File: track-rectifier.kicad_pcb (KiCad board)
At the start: 2 copper layers, 25 x 40 mm, 16 parts, among them J1 PAD, J2 MPB1, J3 Screw_Terminal_01x02, J4 PAD, J5 MPB1

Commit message: Change name to "Track Rectifier".
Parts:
- D3: footprint track-voltage:S250 -> track-rectifier:S250
- J2, J5: footprint track-voltage:MPB1 -> track-rectifier:MPB1
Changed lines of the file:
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@@
     (add_net VCC)
   )
-  (module track-voltage:MPB1 (layer F.Cu)
+  (module track-rectifier:MPB1 (layer F.Cu)
     (at 172.72 91.44 90)
     (fp_text reference J5 (at 5.334 3.302 90) (layer F.SilkS)
@@
       (net 6 /K) (zone_connect 2))
   )
-  (module track-voltage:MPB1 (layer F.Cu)
+  (module track-rectifier:MPB1 (layer F.Cu)
     (at 192.405 91.44 90)
     (fp_text reference J2 (at 5.334 -3.048 90) (layer F.SilkS)
@@
       (net 4 /J) (zone_connect 2))
   )
-  (module track-voltage:S250 (layer F.Cu)
+  (module track-rectifier:S250 (layer F.Cu)
     (at 182.372 102.362 270)
     (fp_text reference D3 (at 0 4.318 180) (layer F.SilkS)

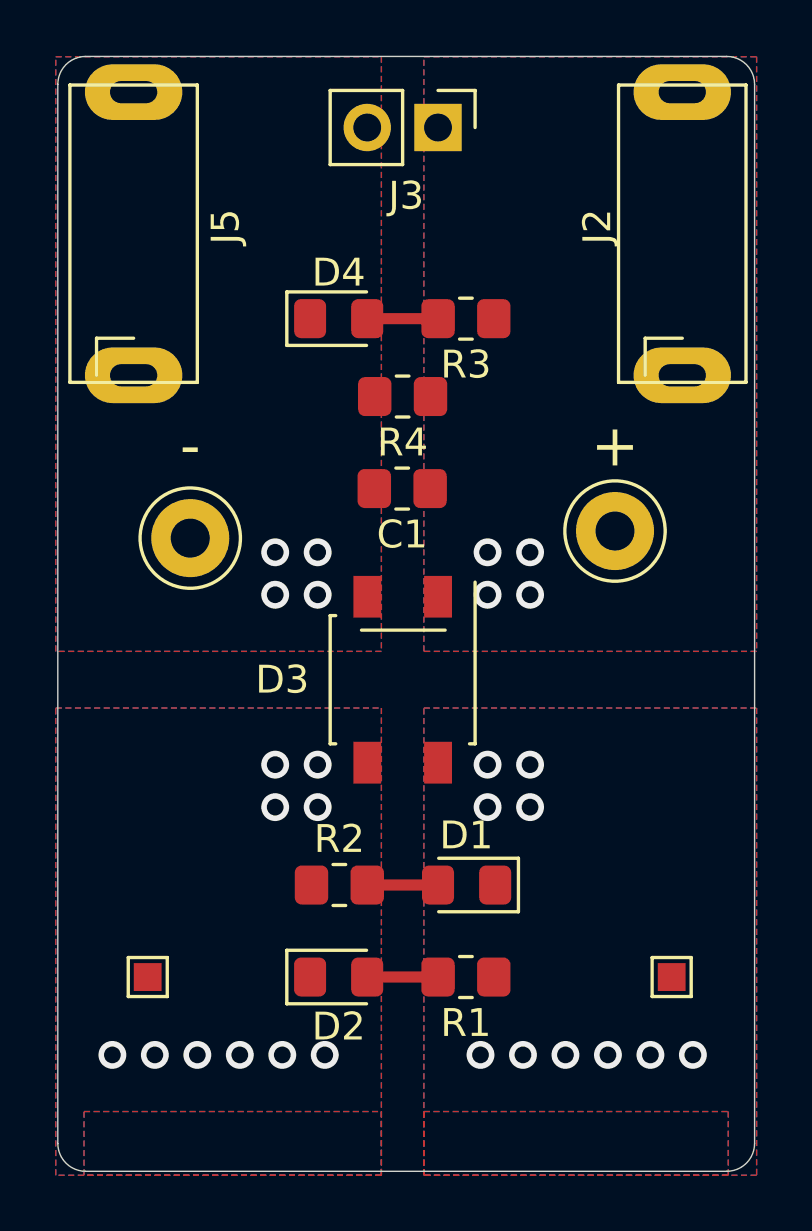
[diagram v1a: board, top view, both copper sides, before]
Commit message: Add PTC on inputs.
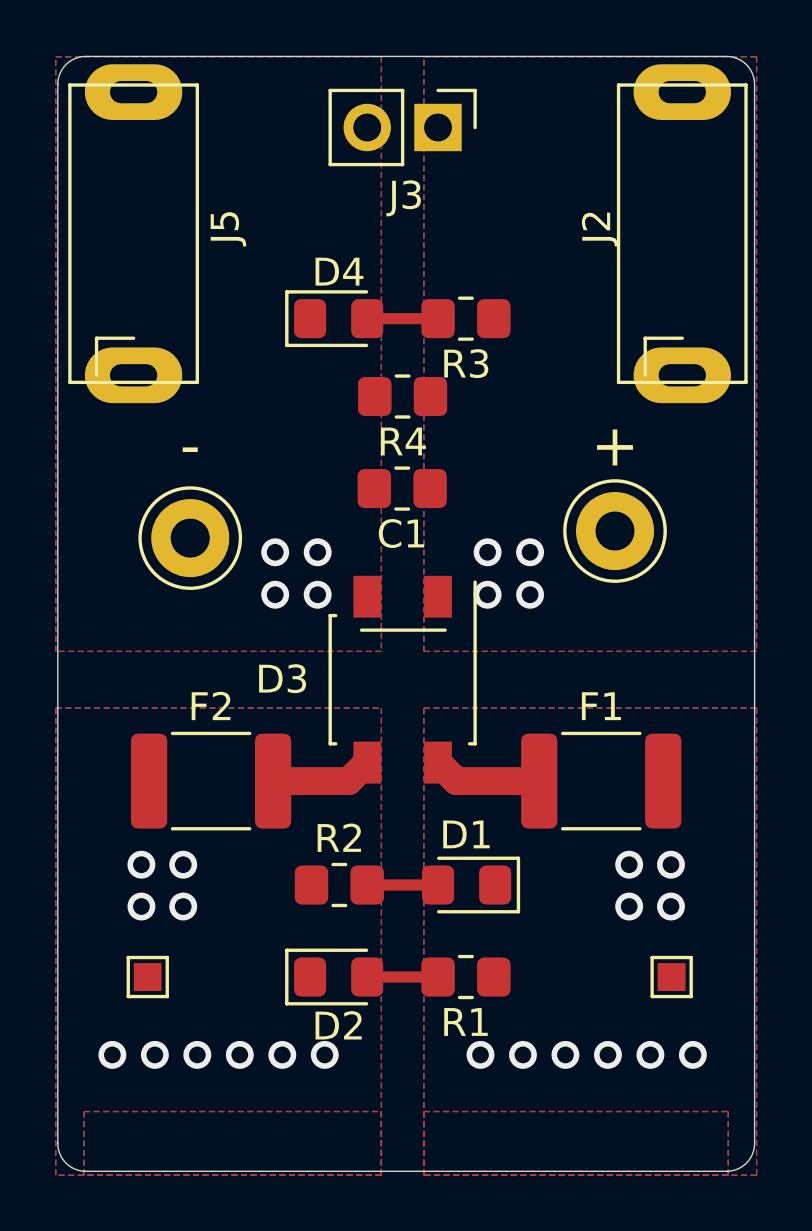
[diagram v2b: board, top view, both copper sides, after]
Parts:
- added F1: 500mA, Fuse:Fuse_1812_4532Metric_Pad1.30x3.40mm_HandSolder, F.Cu at (189.5, 106.0)
- added F2: 500mA, Fuse:Fuse_1812_4532Metric_Pad1.30x3.40mm_HandSolder, F.Cu at (175.5, 106.0)
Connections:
- D3 pad 3: /K -> Net-(D3-Pad3)
- D3 pad 4: /J -> Net-(D3-Pad4)
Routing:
- net Net-(D3-Pad4): track 0.00 -> 3.91 mm
- net Net-(D3-Pad3): track 0.00 -> 3.65 mm
